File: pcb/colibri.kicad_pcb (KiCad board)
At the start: 2 copper layers, 160 x 95.2 mm, 92 parts

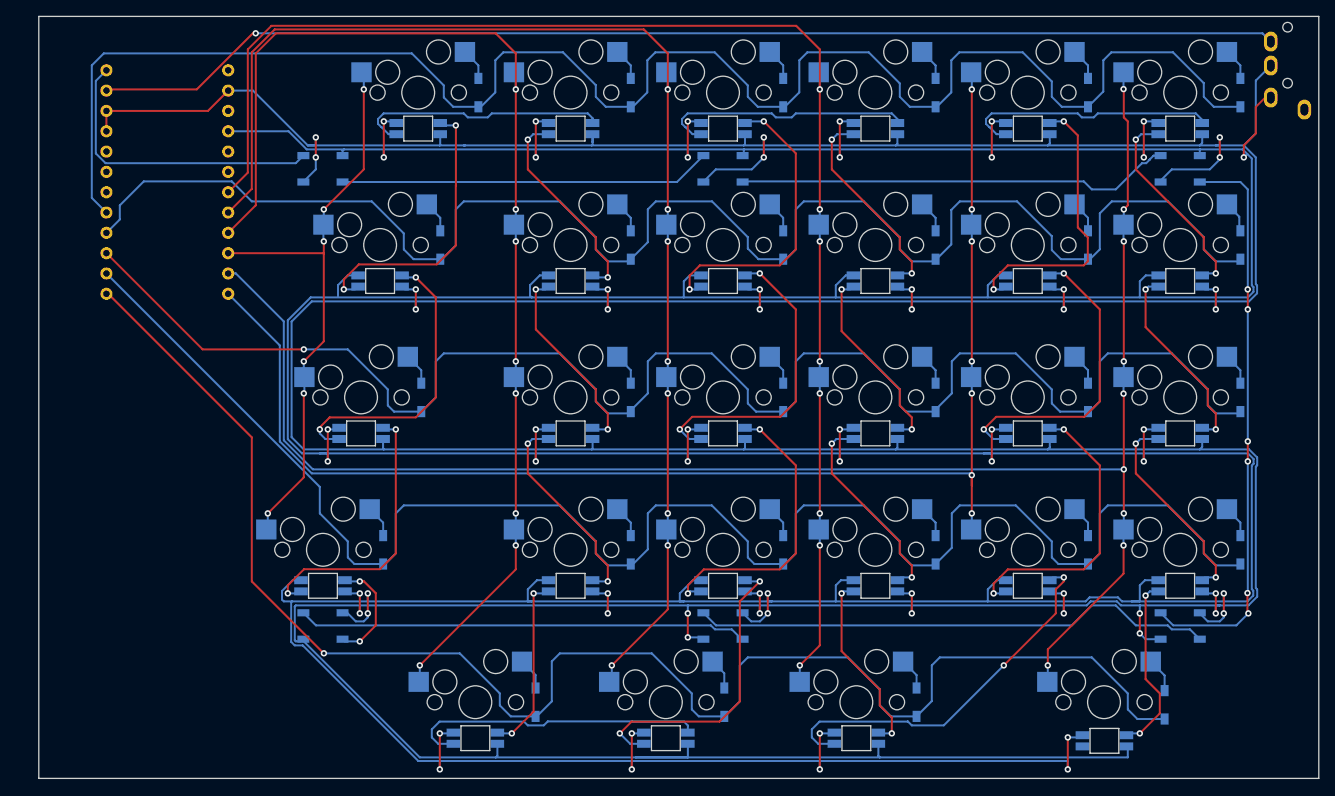
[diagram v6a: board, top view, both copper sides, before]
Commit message: better component placement + more M2 holes
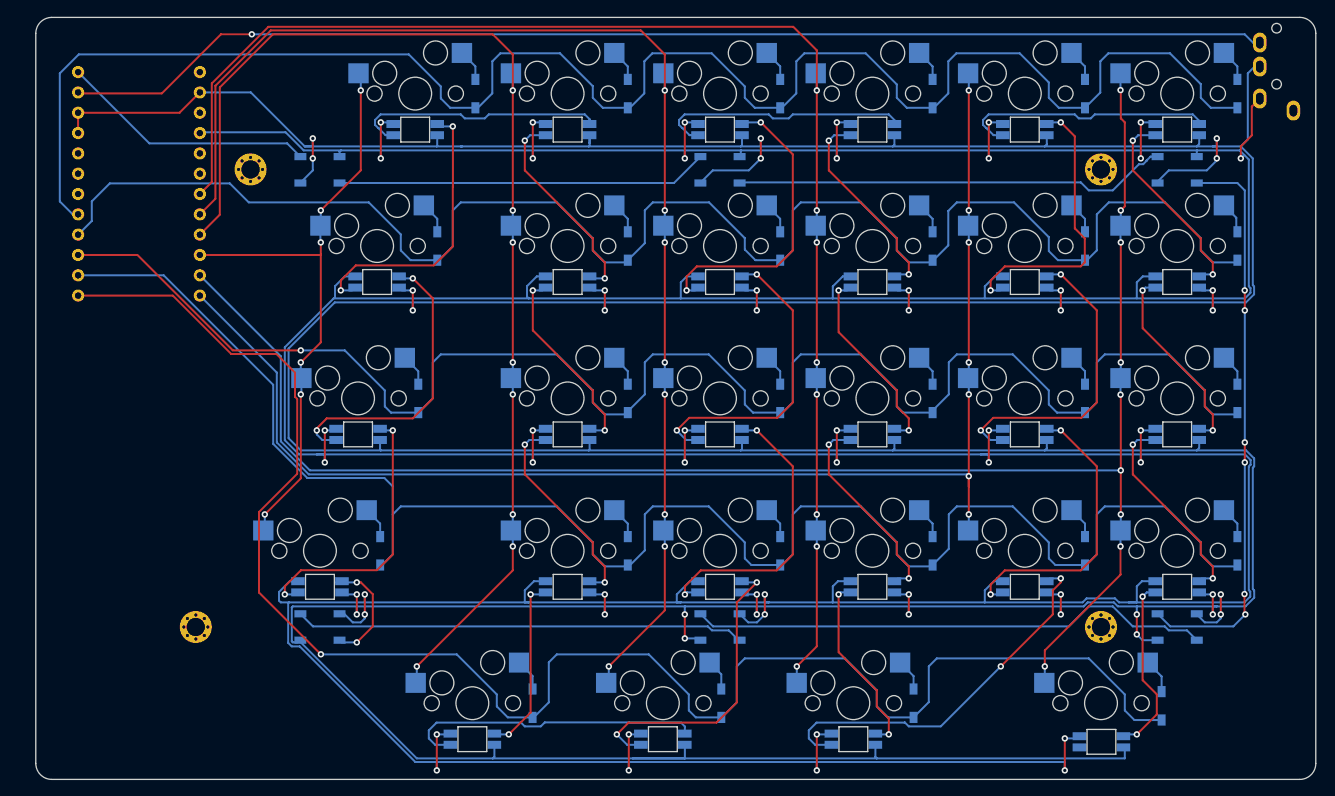
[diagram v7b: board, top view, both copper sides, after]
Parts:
- added Ref**: Val**, kbd:M2_HOLE_v3, F.Cu at (41.0, 116.2)
- added Ref**: Val**, kbd:M2_HOLE_v3, F.Cu at (47.9, 59.0)
- added Ref**: Val**, kbd:M2_HOLE_v3, F.Cu at (154.2, 116.2)
- added Ref**: Val**, kbd:M2_HOLE_v3, F.Cu at (154.2, 59.0)
- moved pro-micro1 3.55 mm to (33.9, 61.3)
- moved ljack-1 1.38 mm to (176.1, 39.9)
- moved ld-1 0.40 mm to (76.0, 49.5)
- moved ld-10 0.40 mm to (133.1, 68.6)
- moved ld-11 0.40 mm to (152.2, 68.6)
- moved ld-12 0.40 mm to (171.2, 68.6)
- moved ld-13 0.40 mm to (68.8, 87.6)
- moved ld-14 0.40 mm to (95.0, 87.6)
- moved ld-15 0.40 mm to (114.0, 87.6)
- moved ld-16 0.40 mm to (133.1, 87.6)
- moved ld-17 0.40 mm to (152.2, 87.6)
- moved ld-18 0.40 mm to (171.2, 87.6)
- moved ld-19 0.40 mm to (64.0, 106.7)
- moved ld-2 0.40 mm to (95.0, 49.5)
- moved ld-20 0.40 mm to (95.0, 106.7)
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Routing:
- net lrow4: track 195.7 -> 211.2 mm
- net lled: track 37.8 -> 32.2 mm
- net lrow3: track 207.9 -> 213.2 mm
- net lrow0: track 210.7 -> 214.5 mm
- net lrow1: track 196.8 -> 200.3 mm
- net lcol0: track 73.5 -> 76.7 mm
- net lrow2: track 198.6 -> 201.8 mm
- net ldata: track 148.7 -> 151.1 mm
- net lcol2: track 157.7 -> 159.1 mm
- net lcol3: track 174.1 -> 175.5 mm
- net lcol1: track 142.3 -> 143.7 mm
- net lcol4: track 167.3 -> 168.5 mm
- net lVCC: track 851.8 -> 853.0 mm
- net lcol5: track 210.8 -> 211.9 mm
- net lGND: track 827.6 -> 828.2 mm
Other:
- outline, holes or cut-outs redrawn

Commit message: reset button
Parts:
- added lreset-1: SW_PUSH, kbd:ResetSW_4P, B.Cu at (34.2, 91.3)
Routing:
- net lreset: track 0.00 -> 65.4 mm
- net lGND: track 828.2 -> 877.6 mm
- net lrow1: track 200.3 -> 198.9 mm
